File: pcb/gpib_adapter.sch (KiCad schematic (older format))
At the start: 27 parts, among them IC1 ATMEGA16U4, P1 ISP, P2 USB, P3 GPIO, P4 UART, P5 GPIB, P6 PWR_JMP, U1 SN75160, U2 SN75161

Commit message: Fixed GPIB pin 17, missing trace, added gerbers to plot folder
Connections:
- net REN B: now also P5.17 (P17)
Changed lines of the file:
@@
-EESchema Schematic File Version 2  date Sun 15 Jul 2012 06:25:58 PM EEST
+EESchema Schematic File Version 2  date Sun 15 Jul 2012 10:44:39 PM EEST
 LIBS:power
 LIBS:device
@@
 	9100 3100 9500 3100
 Wire Bus Line
-	9000 2200 9000 3000
+	9000 2200 9000 3100
 Wire Bus Line
 	8000 2200 8000 5200
@@
 Wire Wire Line
 	2050 2300 2250 2300
+Text Label 9150 3200 0    60   ~ 0
+REN B
+Entry Wire Line
+	9000 3100 9100 3200
+Wire Wire Line
+	9100 3200 9500 3200
 $EndSCHEMATC

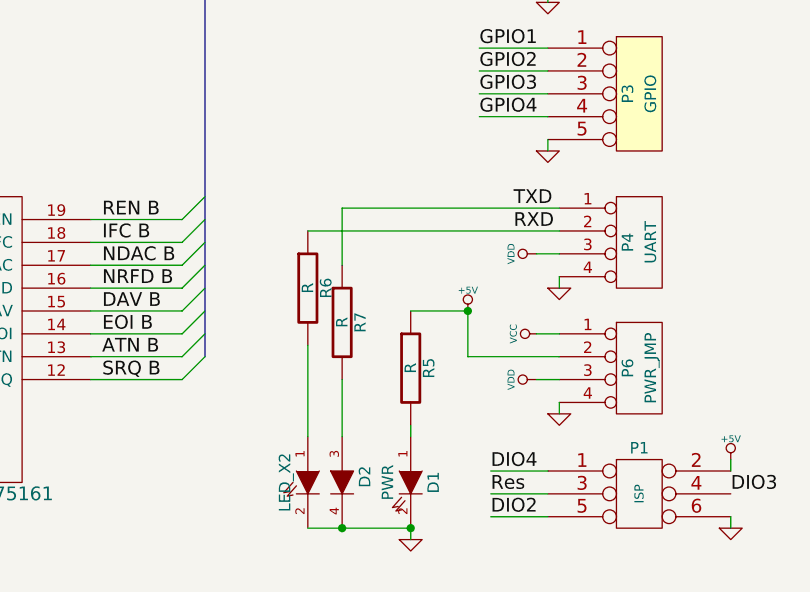
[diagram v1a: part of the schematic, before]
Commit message: Did loads of fine tuning, added mounting holes, rerouted GPIO and UART headers, changed board dimensions
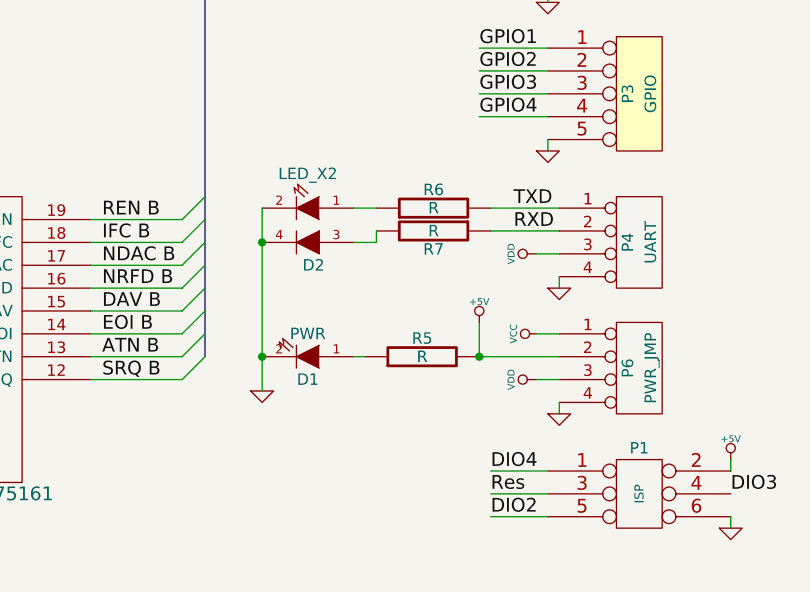
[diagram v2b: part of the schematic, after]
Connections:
- net +5V: now also R5.2; no longer R5.1
- net RXD: now also R7.1; no longer R6.1
- net TXD: now also R6.2; no longer R7.1
- net at D1.1 (A): now also R5.1; no longer R5.2
- net at D2.1 (A): now also R6.1; no longer R6.2
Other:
- moved on the sheet: D1, D2, R5, R6, R7
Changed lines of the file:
@@
-EESchema Schematic File Version 2  date Sun 15 Jul 2012 10:44:39 PM EEST
+EESchema Schematic File Version 2  date Mon 16 Jul 2012 01:56:33 PM EEST
 LIBS:power
 LIBS:device
@@
 Sheet 1 1
 Title ""
-Date "15 jul 2012"
+Date "16 jul 2012"
 Rev ""
 Comp ""
@@
 L +5V #PWR016
 U 1 1 5001DC92
-P 9150 5000
-F 0 "#PWR016" H 9150 5090 20  0001 C CNN
-F 1 "+5V" H 9150 5090 30  0000 C CNN
-	1    9150 5000
+P 9200 5050
+F 0 "#PWR016" H 9200 5140 20  0001 C CNN
+F 1 "+5V" H 9200 5140 30  0000 C CNN
+	1    9200 5050
 	1    0    0    -1
 $EndComp
@@
 Wire Bus Line
 	8000 2200 8000 5200
-Wire Bus Line
-	8000 2200 10800 2200
 Wire Wire Line
 	9100 2600 9500 2600
@@
 L LED D1
 U 1 1 50027DF1
-P 8900 5750
-F 0 "D1" H 8900 5850 50  0000 C CNN
-F 1 "PWR" H 8900 5650 50  0000 C CNN
-F 3 "datasheets/APT1608QBC-D.pdf" H 8900 5750 60  0001 C CNN
-	1    8900 5750
-	0    1    1    0
+P 8450 5200
+F 0 "D1" H 8450 5300 50  0000 C CNN
+F 1 "PWR" H 8450 5100 50  0000 C CNN
+F 3 "datasheets/APT1608QBC-D.pdf" H 8450 5200 60  0001 C CNN
+	1    8450 5200
+	-1   0    0    1
 $EndComp
 $Comp
 L R R5
 U 1 1 50027E00
-P 8900 5250
-F 0 "R5" V 8980 5250 50  0000 C CNN
-F 1 "R" V 8900 5250 50  0000 C CNN
-	1    8900 5250
-	1    0    0    -1
-$EndComp
-Wire Wire Line
-	9550 5200 9150 5200
-Wire Wire Line
-	9150 5200 9150 5000
+P 8950 5200
+F 0 "R5" V 9030 5200 50  0000 C CNN
+F 1 "R" V 8950 5200 50  0000 C CNN
+	1    8950 5200
+	0    -1   -1   0
+$EndComp
 $Comp
 L GND #PWR024
 U 1 1 50027FCC
-P 8900 6000
-F 0 "#PWR024" H 8900 6000 30  0001 C CNN
-F 1 "GND" H 8900 5930 30  0001 C CNN
-	1    8900 6000
-	1    0    0    -1
-$EndComp
-Wire Wire Line
-	8900 5950 8900 6000
-Wire Wire Line
-	8900 5550 8900 5500
-Wire Wire Line
-	9150 5000 8900 5000
-Connection ~ 9150 5000
+P 8250 5350
+F 0 "#PWR024" H 8250 5350 30  0001 C CNN
+F 1 "GND" H 8250 5280 30  0001 C CNN
+	1    8250 5350
+	1    0    0    -1
+$EndComp
 $Comp
 L R R7
 U 1 1 50028616
-P 8600 5050
-F 0 "R7" V 8680 5050 50  0000 C CNN
-F 1 "R" V 8600 5050 50  0000 C CNN
-	1    8600 5050
-	1    0    0    -1
+P 9000 4650
+F 0 "R7" V 9080 4650 50  0000 C CNN
+F 1 "R" V 9000 4650 50  0000 C CNN
+	1    9000 4650
+	0    1    1    0
 $EndComp
 $Comp
 L LED_X2 D2
 U 1 1 500289DC
-P 8450 5750
-F 0 "D2" H 8425 6000 50  0000 C CNN
-F 1 "LED_X2" H 8450 5650 50  0000 C CNN
-F 3 "datasheets/APTB1612YSGC-F01.pdf" H 8450 5750 60  0001 C CNN
-	1    8450 5750
-	0    1    1    0
-$EndComp
-Wire Wire Line
-	8600 5550 8600 5300
+P 8450 4550
+F 0 "D2" H 8425 4800 50  0000 C CNN
+F 1 "LED_X2" H 8450 4400 50  0000 C CNN
+F 3 "datasheets/APTB1612YSGC-F01.pdf" H 8450 4550 60  0001 C CNN
+	1    8450 4550
+	-1   0    0    1
+$EndComp
 $Comp
 L R R6
 U 1 1 50028B33
-P 8450 4900
-F 0 "R6" V 8530 4900 50  0000 C CNN
-F 1 "R" V 8450 4900 50  0000 C CNN
-	1    8450 4900
-	1    0    0    -1
-$EndComp
-Wire Wire Line
-	8450 5550 8450 5150
-Wire Wire Line
-	8450 5950 8900 5950
-Connection ~ 8600 5950
-Connection ~ 8900 5950
-Wire Wire Line
-	8600 4800 8600 4550
-Wire Wire Line
-	8600 4550 9550 4550
-Wire Wire Line
-	8450 4650 9550 4650
+P 9000 4550
+F 0 "R6" V 9080 4550 50  0000 C CNN
+F 1 "R" V 9000 4550 50  0000 C CNN
+	1    9000 4550
+	0    -1   -1   0
+$EndComp
 Connection ~ 3700 2000
 Connection ~ 3850 5550
@@
 Wire Wire Line
 	9100 3200 9500 3200
+Wire Wire Line
+	9250 4550 9550 4550
+Wire Wire Line
+	9250 4650 9550 4650
+Wire Wire Line
+	8650 4550 8750 4550
+Wire Wire Line
+	8650 4700 8750 4700
+Wire Wire Line
+	8750 4700 8750 4650
+Wire Wire Line
+	9550 5200 9200 5200
+Wire Wire Line
+	9200 5200 9200 5050
+Connection ~ 9200 5200
+Wire Wire Line
+	8700 5200 8650 5200
+Wire Wire Line
+	8250 4550 8250 5350
+Connection ~ 8250 4700
+Connection ~ 8250 5200
+Wire Bus Line
+	8000 2200 10800 2200
 $EndSCHEMATC
